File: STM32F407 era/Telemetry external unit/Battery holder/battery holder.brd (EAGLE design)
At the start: 65 x 56 mm, 1 part

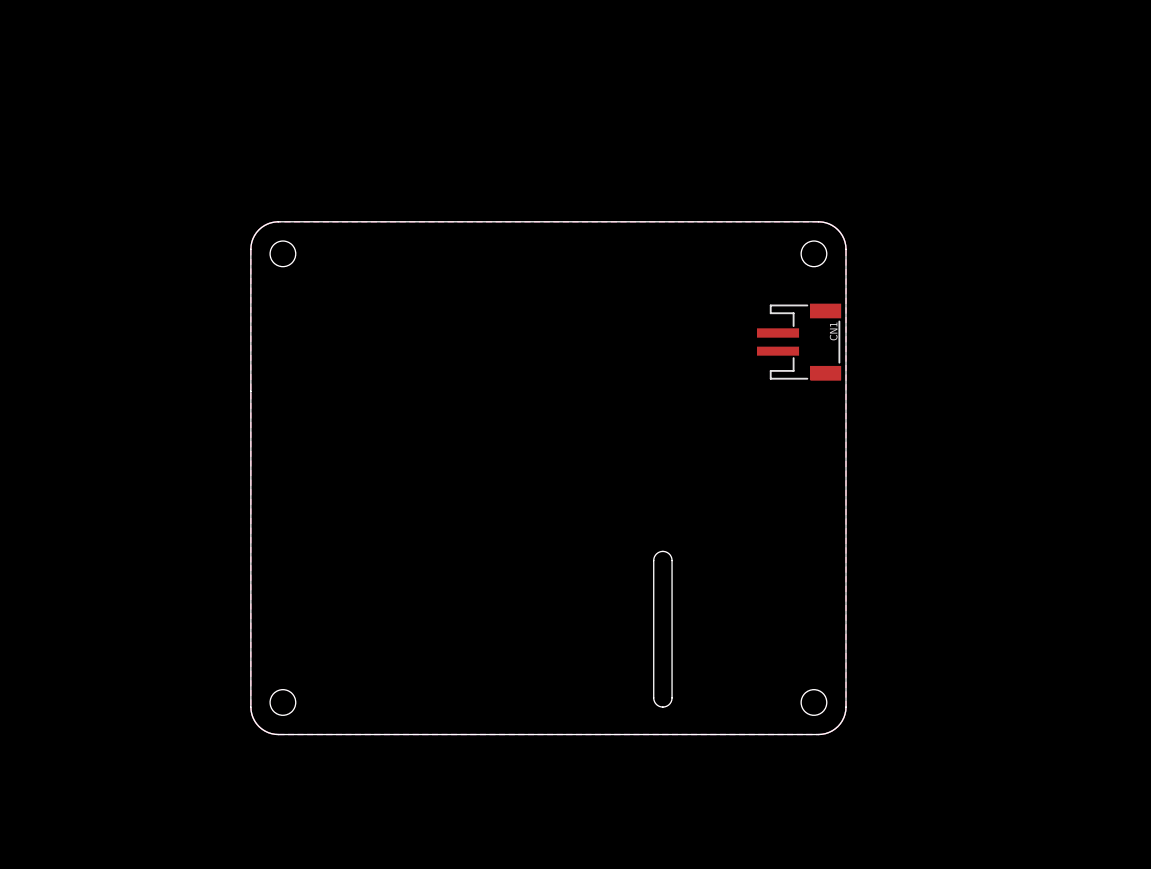
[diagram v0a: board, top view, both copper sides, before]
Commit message: changes to battery board
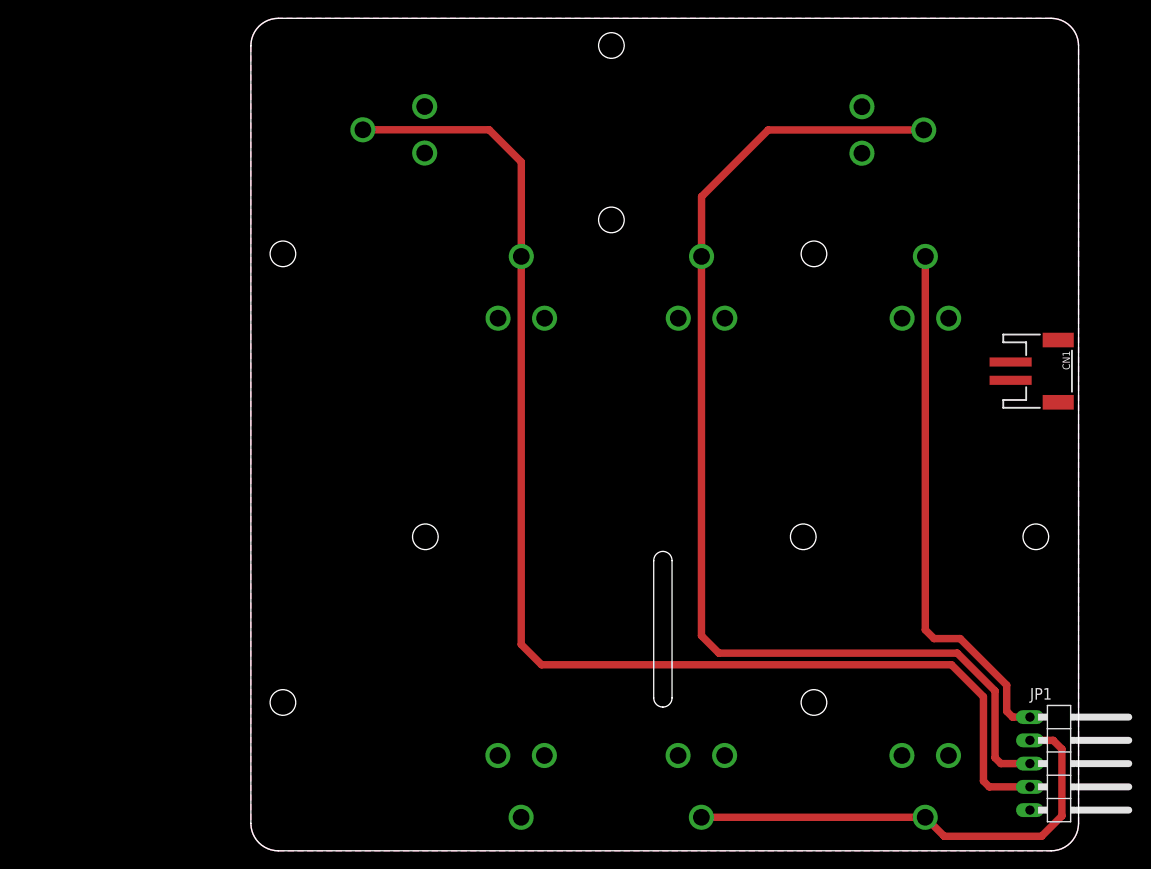
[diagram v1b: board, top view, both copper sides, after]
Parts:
- added BAT1, BAT2, BAT3, BAT4: (no value), SparkFun-Electromechanical:BATTERY_18650-HOLDER
- added JP1: (no value), pinhead:1X05/90
- moved CN1 25.6 mm to (86.7, 39.7)
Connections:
- new net 12V: BAT1.PWR@1, JP1.1
- new net N$1: BAT1.GND@1, BAT2.PWR@1, JP1.2
- new net N$2: BAT2.GND@1, BAT3.PWR@1, JP1.3
- new net N$3: BAT3.GND@1, BAT4.PWR@1, JP1.4
- net GND: now also BAT4.GND@1, JP1.5
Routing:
- net N$3: track 0.00 -> 138.9 mm
- net N$2: track 0.00 -> 121.2 mm
- net 12V: track 0.00 -> 57.8 mm
- net N$1: track 0.00 -> 52.3 mm
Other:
- board size 65 x 56 mm -> 90.4 x 90.9 mm

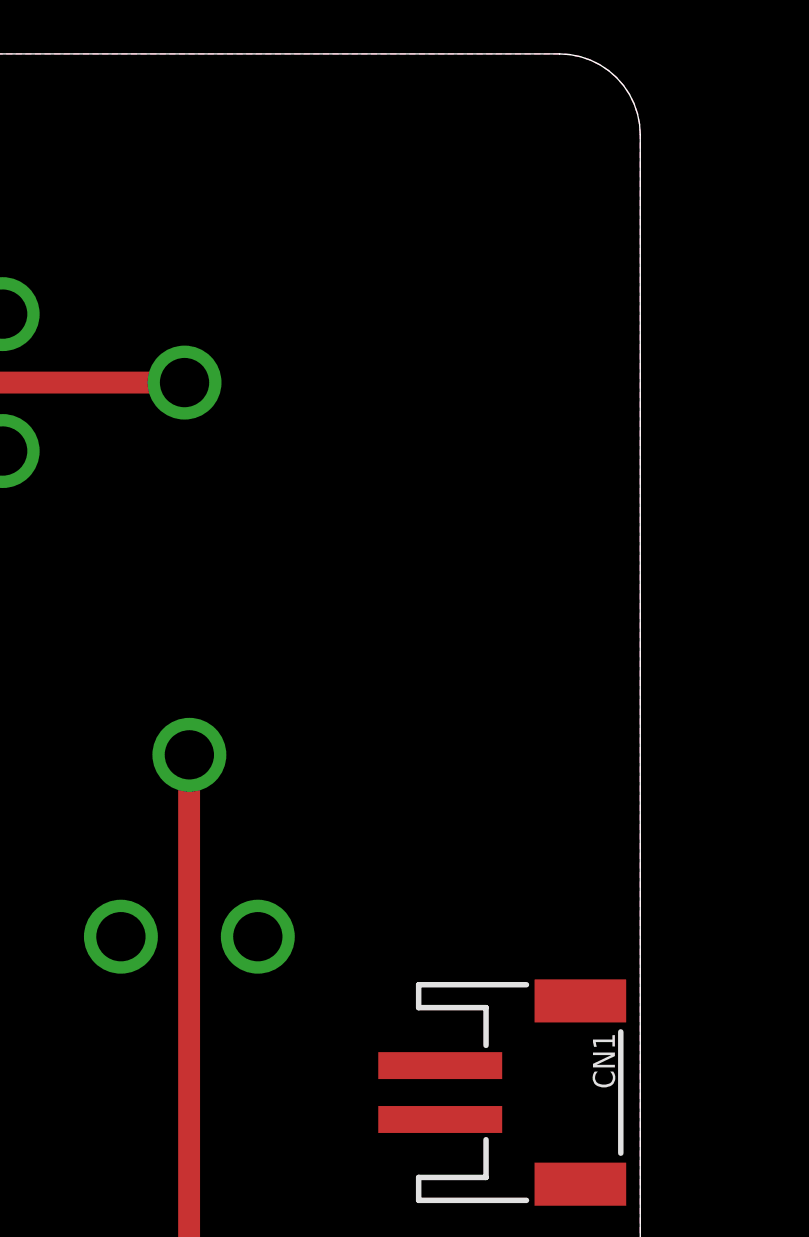
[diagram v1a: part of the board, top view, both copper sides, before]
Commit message: added Switching power supply to telemtry battery board
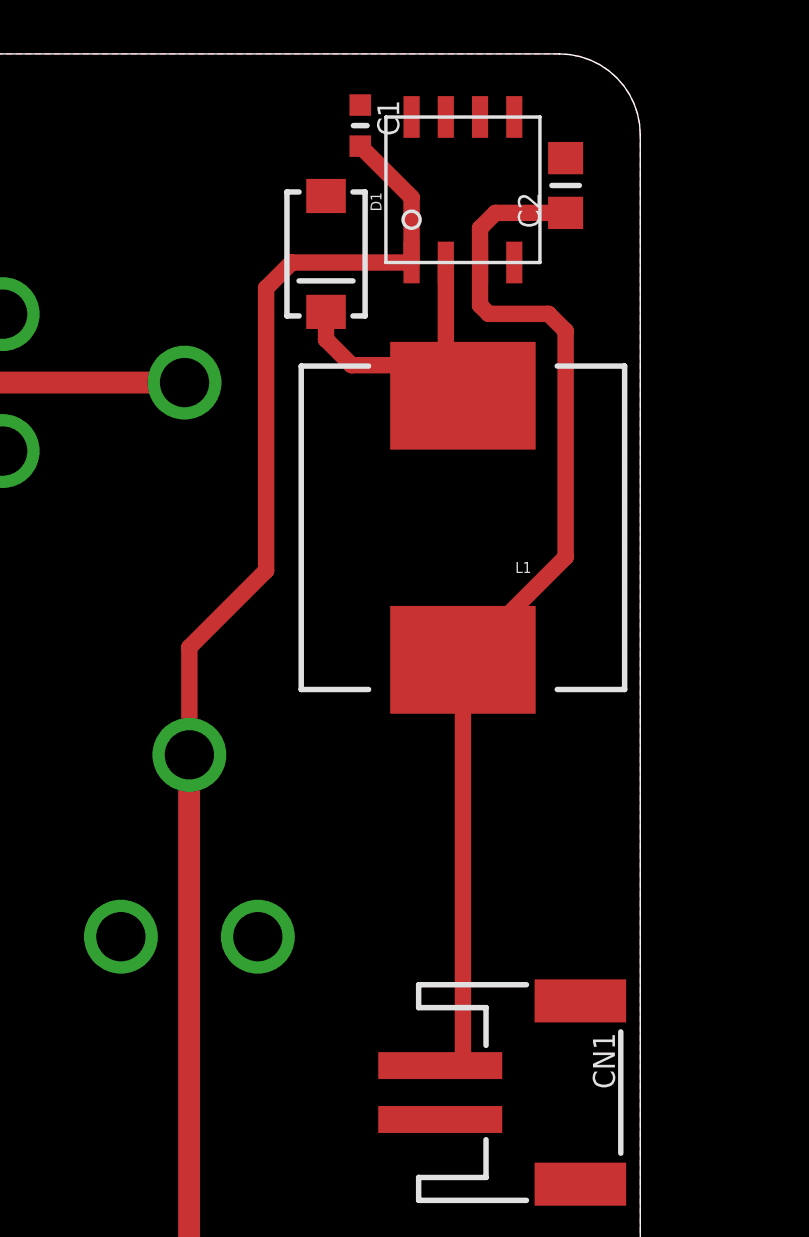
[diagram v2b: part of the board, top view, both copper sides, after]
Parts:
- added C1: 100n, microbuilder:_0603MP
- added C2: 10u, microbuilder:_0805MP
- added D1: B340A-13-F, SparkFun-DiscreteSemi:SMA-DIODE
- added L1: MSS1038-473MLC 47u, SparkFun-Passives:CDRH125
- added U$3: AP1509, unicorn_v2:SOP-8L
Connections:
- new net N$6: D1.C, L1.2, U$3.P$2
- net +5V: now also C2.1, L1.1, U$3.P$3
- net 12V: now also C1.2, U$3.P$1
- net GND: now also C1.1, C2.2, D1.A, U$3.P$4, U$3.P$5, U$3.P$6, U$3.P$7, U$3.P$8
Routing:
- net +5V: track 0.00 -> 39.6 mm
- net 12V: track 57.8 -> 87.2 mm
- net N$6: track 0.00 -> 11.6 mm
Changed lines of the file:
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@@
 <setting verticaltext="up"/>
 </settings>
-<grid distance="0.125" unitdist="inch" unit="inch" style="lines" multiple="1" display="yes" altdistance="0.025" altunitdist="inch" altunit="inch"/>
+<grid distance="0.0125" unitdist="inch" unit="inch" style="lines" multiple="1" display="yes" altdistance="0.025" altunitdist="inch" altunit="inch"/>
 <layers>
 <layer number="1" name="Top" color="4" fill="1" visible="yes" active="yes"/>
@@
 <layer number="56" name="wert" color="7" fill="1" visible="no" active="no"/>
 <layer number="57" name="tCAD" color="7" fill="1" visible="no" active="no"/>
+<layer number="90" name="Modules" color="5" fill="1" visible="yes" active="yes"/>
 <layer number="91" name="Nets" color="2" fill="1" visible="no" active="no"/>
 <layer number="92" name="Busses" color="1" fill="1" visible="no" active="no"/>
@@
 <element name="BAT4" library="SparkFun-Electromechanical" package="BATTERY_18650-HOLDER" value="" x="29.5275" y="21.59" rot="MR270"/>
 <element name="JP1" library="pinhead" package="1X05/90" value="" x="88.9" y="-3.175" rot="R270"/>
+<element name="U$3" library="unicorn_v2" package="SOP-8L" value="AP1509" x="83.82" y="73.025"/>
+<element name="C1" library="microbuilder" package="_0603MP" value="100n" x="80.01" y="75.565" rot="R270"/>
+<element name="C2" library="microbuilder" package="_0805MP" value="10u" x="87.63" y="73.3425" rot="R90"/>
+<element name="L1" library="SparkFun-Passives" package="CDRH125" value="MSS1038-473MLC 47u" x="83.82" y="60.6425" rot="R180"/>
+<element name="D1" library="SparkFun-DiscreteSemi" package="SMA-DIODE" value="B340A-13-F" x="78.74" y="70.8025" rot="R270"/>
 </elements>
 <signals>
@@
 <contactref element="JP1" pad="5"/>
 <contactref element="BAT4" pad="GND@1"/>
+<contactref element="U$3" pad="P$5"/>
+<contactref element="U$3" pad="P$6"/>
+<contactref element="U$3" pad="P$7"/>
+<contactref element="U$3" pad="P$8"/>
+<contactref element="U$3" pad="P$4"/>
+<contactref element="C1" pad="1"/>
+<contactref element="C2" pad="2"/>
+<contactref element="D1" pad="A"/>
 </signal>
 <signal name="+5V">
 <contactref element="CN1" pad="1"/>
+<contactref element="U$3" pad="P$3"/>
+<contactref element="C2" pad="1"/>
+<contactref element="L1" pad="1"/>
+<wire x1="87.63" y1="72.3265" x2="85.0265" y2="72.3265" width="0.6096" layer="1"/>
+<wire x1="85.0265" y1="72.3265" x2="84.455" y2="71.755" width="0.6096" layer="1"/>
+<wire x1="84.455" y1="71.755" x2="84.455" y2="70.485" width="0.6096" layer="1"/>
+<wire x1="84.455" y1="70.485" x2="84.455" y2="68.8975" width="0.6096" layer="1"/>
+<wire x1="84.455" y1="68.8975" x2="84.7725" y2="68.58" width="0.6096" layer="1"/>
+<wire x1="84.7725" y1="68.58" x2="86.995" y2="68.58" width="0.6096" layer="1"/>
+<wire x1="86.995" y1="68.58" x2="87.63" y2="67.945" width="0.6096" layer="1"/>
+<wire x1="87.63" y1="67.945" x2="87.63" y2="59.5525" width="0.6096" layer="1"/>
+<wire x1="87.63" y1="59.5525" x2="83.82" y2="55.7425" width="0.6096" layer="1"/>
+<wire x1="83.82" y1="55.7425" x2="83.82" y2="40.64" width="0.6096" layer="1"/>
+<wire x1="83.82" y1="40.64" x2="83.025" y2="40.64" width="0.6096" layer="1"/>
+<wire x1="83.025" y1="40.64" x2="82.9775" y2="40.6875" width="0.6096" layer="1"/>
 </signal>
 <signal name="N$1">
@@
 <wire x1="73.66" y1="11.43" x2="73.66" y2="52.208" width="0.8128" layer="1"/>
 <wire x1="73.66" y1="52.208" x2="73.67" y2="52.218" width="0.8128" layer="1"/>
+<contactref element="U$3" pad="P$1"/>
+<contactref element="C1" pad="2"/>
+<wire x1="73.67" y1="52.218" x2="73.67" y2="56.2075" width="0.6096" layer="1"/>
+<wire x1="73.67" y1="56.2075" x2="76.5175" y2="59.055" width="0.6096" layer="1"/>
+<wire x1="76.5175" y1="59.055" x2="76.5175" y2="69.5325" width="0.6096" layer="1"/>
+<wire x1="76.5175" y1="69.5325" x2="77.47" y2="70.485" width="0.6096" layer="1"/>
+<wire x1="77.47" y1="70.485" x2="81.915" y2="70.485" width="0.6096" layer="1"/>
+<wire x1="81.915" y1="70.485" x2="81.915" y2="72.898" width="0.6096" layer="1"/>
+<wire x1="81.915" y1="72.898" x2="80.01" y2="74.803" width="0.6096" layer="1"/>
+</signal>
+<signal name="N$6">
+<contactref element="L1" pad="2"/>
+<contactref element="U$3" pad="P$2"/>
+<contactref element="D1" pad="C"/>
+<wire x1="83.185" y1="70.485" x2="83.185" y2="67.13" width="0.6096" layer="1"/>
+<wire x1="83.185" y1="67.13" x2="83.82" y2="65.5425" width="0.6096" layer="1"/>
+<wire x1="78.74" y1="68.6525" x2="78.74" y2="67.6275" width="0.6096" layer="1"/>
+<wire x1="78.74" y1="67.6275" x2="79.6925" y2="66.675" width="0.6096" layer="1"/>
+<wire x1="79.6925" y1="66.675" x2="83.365" y2="66.675" width="0.6096" layer="1"/>
+<wire x1="83.365" y1="66.675" x2="83.185" y2="67.13" width="0.6096" layer="1"/>
 </signal>
 </signals>

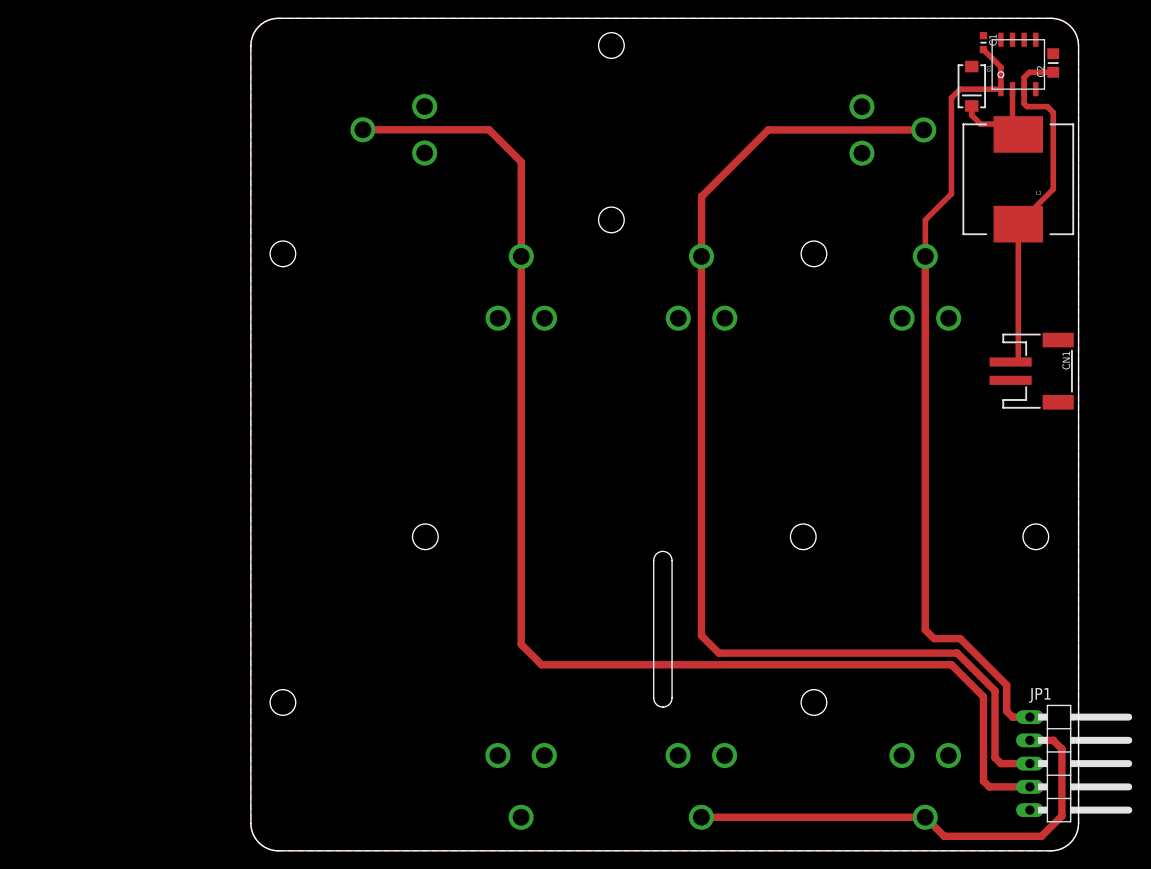
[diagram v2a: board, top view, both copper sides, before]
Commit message: layout updates to fit 2 xbees
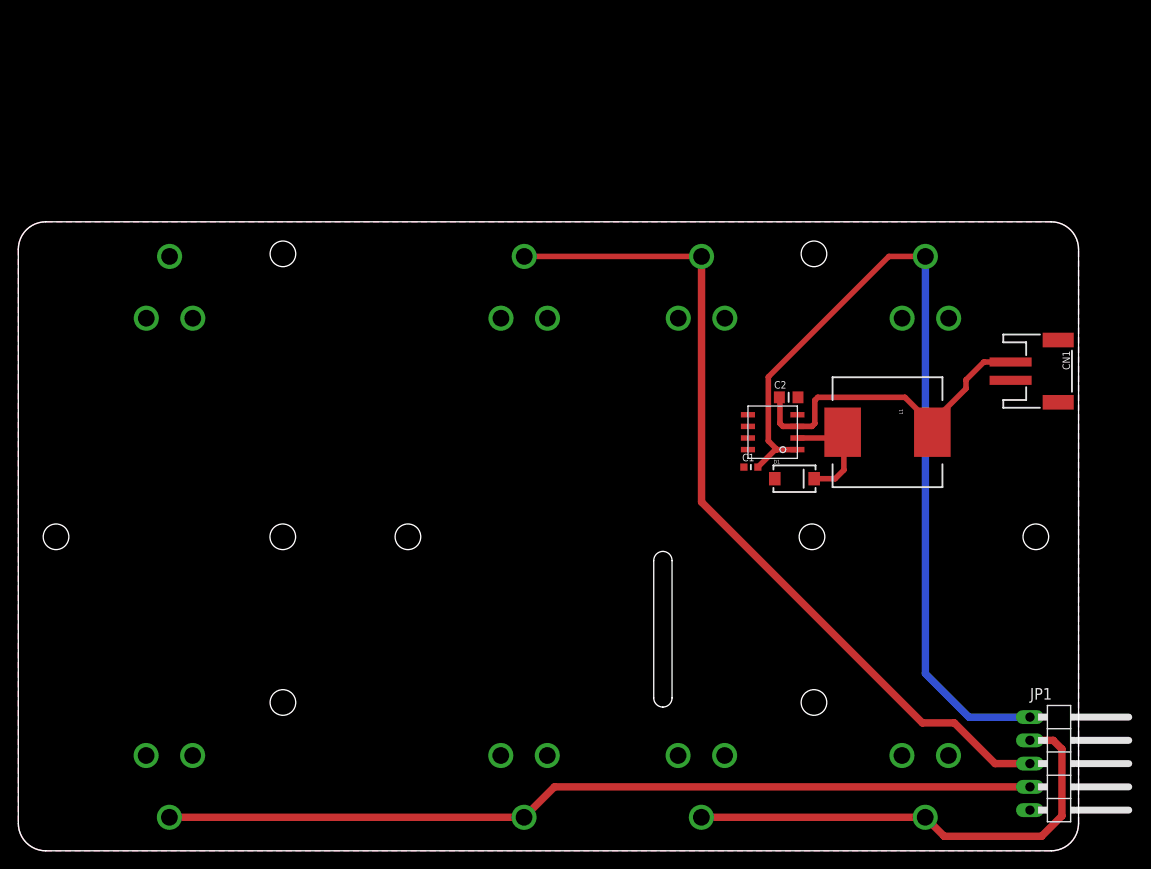
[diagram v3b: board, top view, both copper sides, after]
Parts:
- moved C1 52.9 mm to (54.6, 29.2), turned to 0 degrees
- moved U$3 48.1 mm to (57.1, 33.0), turned to 90 degrees
- moved D1 47.0 mm to (59.4, 27.9), turned to 0 degrees
- moved C2 46.6 mm to (58.7, 36.8), turned to 0 degrees
- moved BAT3 46.3 mm to (29.8, 21.6), turned to 270 degrees
- moved BAT4 38.4 mm to (-8.89, 21.6), turned to 90 degrees
- moved L1 31.1 mm to (69.5, 33.0), turned to 270 degrees
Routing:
- net N$3: track 138.9 -> 95.4 mm
- net N$2: track 121.2 -> 93.9 mm
- net 12V: track 87.2 -> 95.0 mm
- net +5V: track 39.6 -> 37.4 mm
- net N$6: track 11.6 -> 13.1 mm
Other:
- board size 90.4 x 90.9 mm -> 115.8 x 68.7 mm
